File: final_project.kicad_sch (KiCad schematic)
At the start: 12 parts, among them U1 ATmega328-P, U2 SGP30, U3 TXS0102DCT, U3_5V_to_1.8V_Voltage_Regulator ADP3336ARMZ

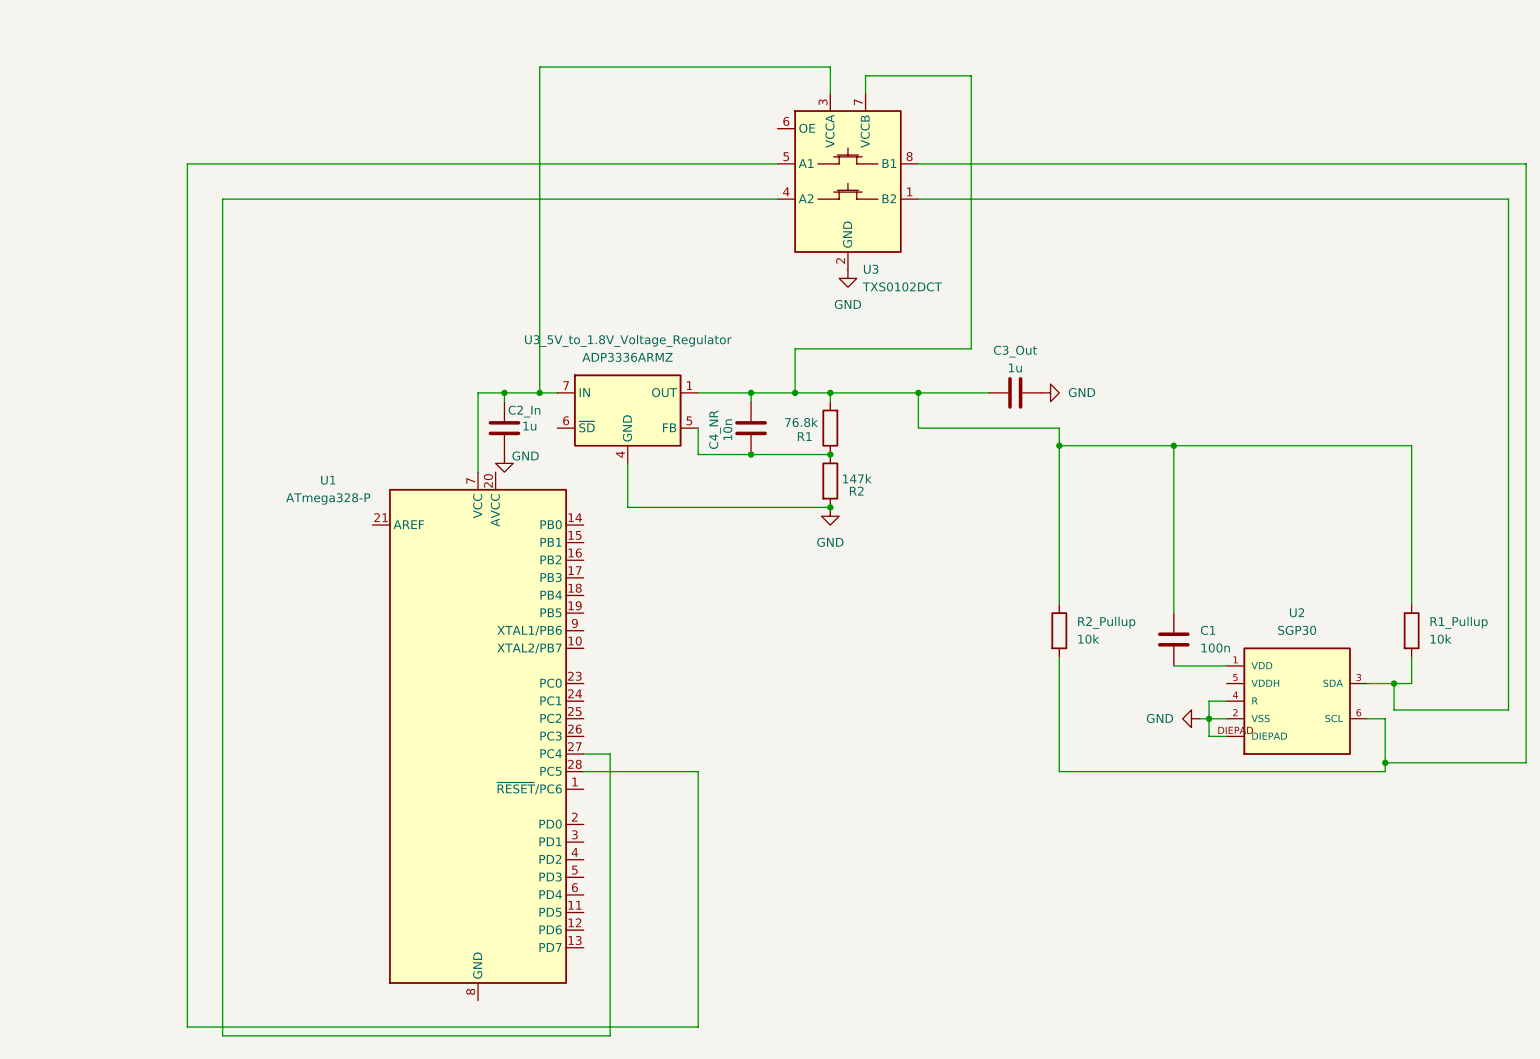
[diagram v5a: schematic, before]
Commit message: Added Global labels
Added Global labels to the level shifter to make it more organized.
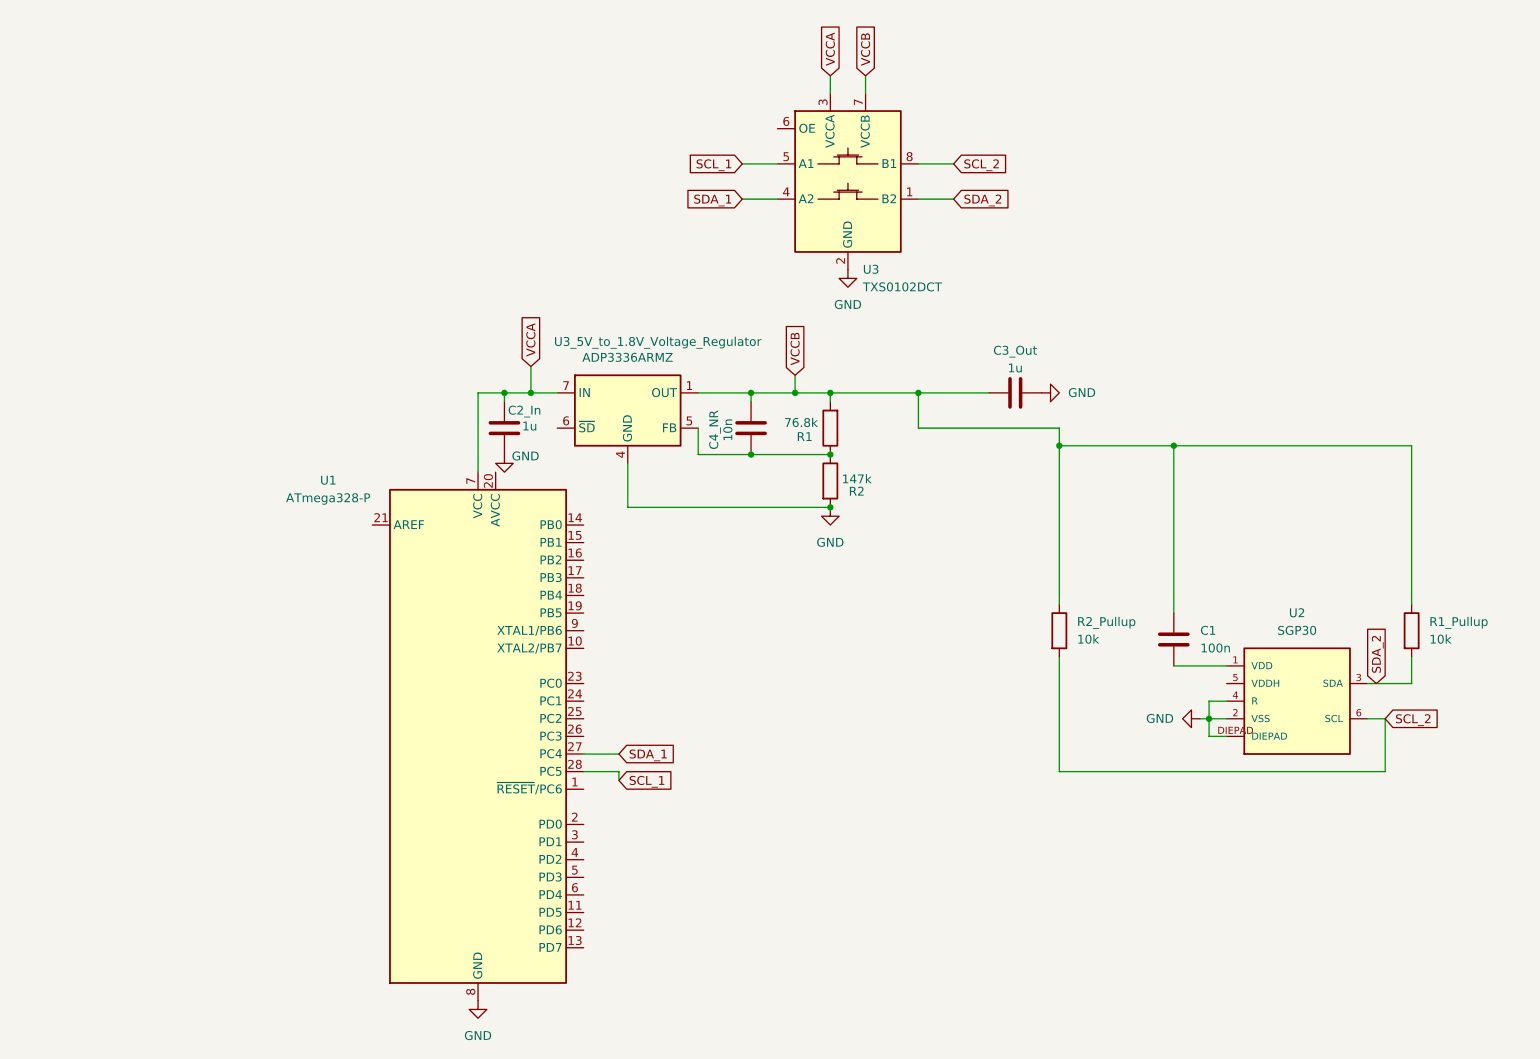
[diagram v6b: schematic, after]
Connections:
- net GND: now also U1.22 (GND), U1.8 (GND)
- net VCCB: now reaches C1.1, C3_Out.1, C4_NR.2, R1.2, R1_Pullup.1, R2_Pullup.1, U3.7 (VCCB), U3_5V_to_1.8V_Voltage_Regulator.1 (OUT), U3_5V_to_1.8V_Voltage_Regulator.2 (OUT), U3_5V_to_1.8V_Voltage_Regulator.3 (OUT)
- net VCCA: now reaches C2_In.1, U1.7 (VCC), U3.3 (VCCA), U3_5V_to_1.8V_Voltage_Regulator.7 (IN), U3_5V_to_1.8V_Voltage_Regulator.8 (IN)
- net SDA_2: now reaches R1_Pullup.2, U2.3 (SDA), U3.1 (B2)
- net SDA_1: now reaches U1.27 (PC4), U3.4 (A2)
- net SCL_1: now reaches U1.28 (PC5), U3.5 (A1)
- net SCL_2: now reaches R2_Pullup.2, U2.6 (SCL), U3.8 (B1)

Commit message: Added the oscillator for Atmega
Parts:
- added C2, C3: 22pF, symbol Device:C
- added Y1: 16 MHz, symbol Device:Crystal
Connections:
- net GND: now also C2.2, C3.1
- net at U1.10 (XTAL2/PB7): now also C3.2, Y1.1
- net at U1.9 (XTAL1/PB6): now also C2.1, Y1.2

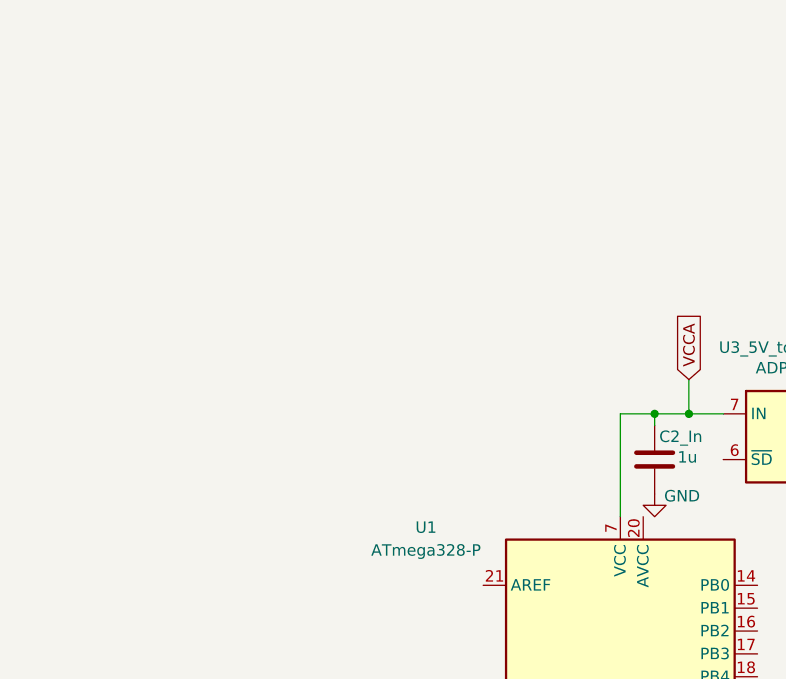
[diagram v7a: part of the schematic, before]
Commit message: Added the battery
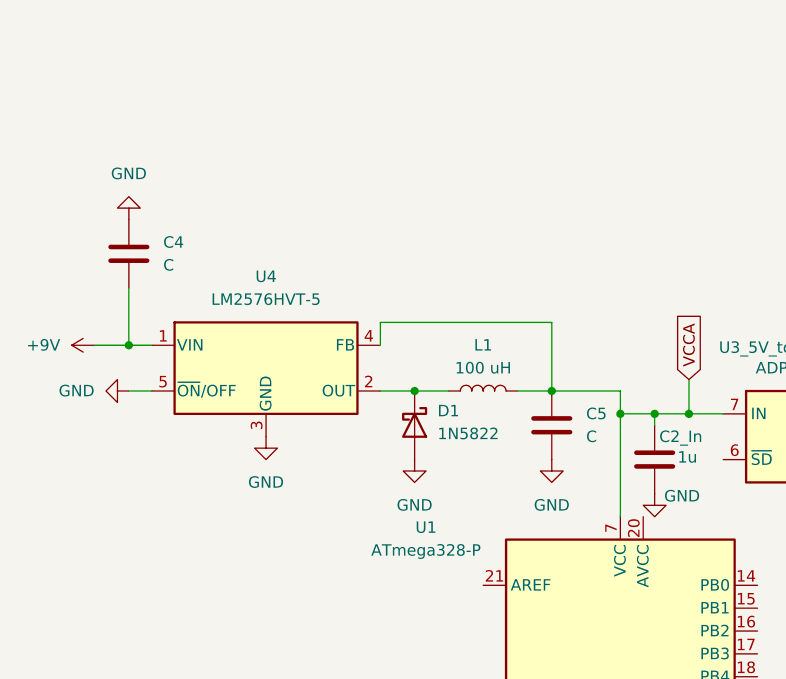
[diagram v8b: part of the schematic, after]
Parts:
- added C4, C5: C, symbol Device:C
- added D1: 1N5822, Diode_THT:D_DO-201AD_P15.24mm_Horizontal, symbol Diode:1N5822
- added L1: 100 uH, symbol Device:L
- added U4: LM2576HVT-5, Package_TO_SOT_THT:TO-220-5_Vertical, symbol Regulator_Switching:LM2576HVT-5
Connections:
- net GND: now also C4.1, C5.2, D1.2 (A), U4.3 (GND), U4.5 (~{ON}/OFF)
- net VCCA: now also C5.1, L1.2, U4.4 (FB)
- new net: D1.1 (K), L1.1, U4.2 (OUT)
- new net +9V: C4.2, U4.1 (VIN)
